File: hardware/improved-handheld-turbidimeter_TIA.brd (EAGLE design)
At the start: 30.1 x 39.4 mm, 11 parts

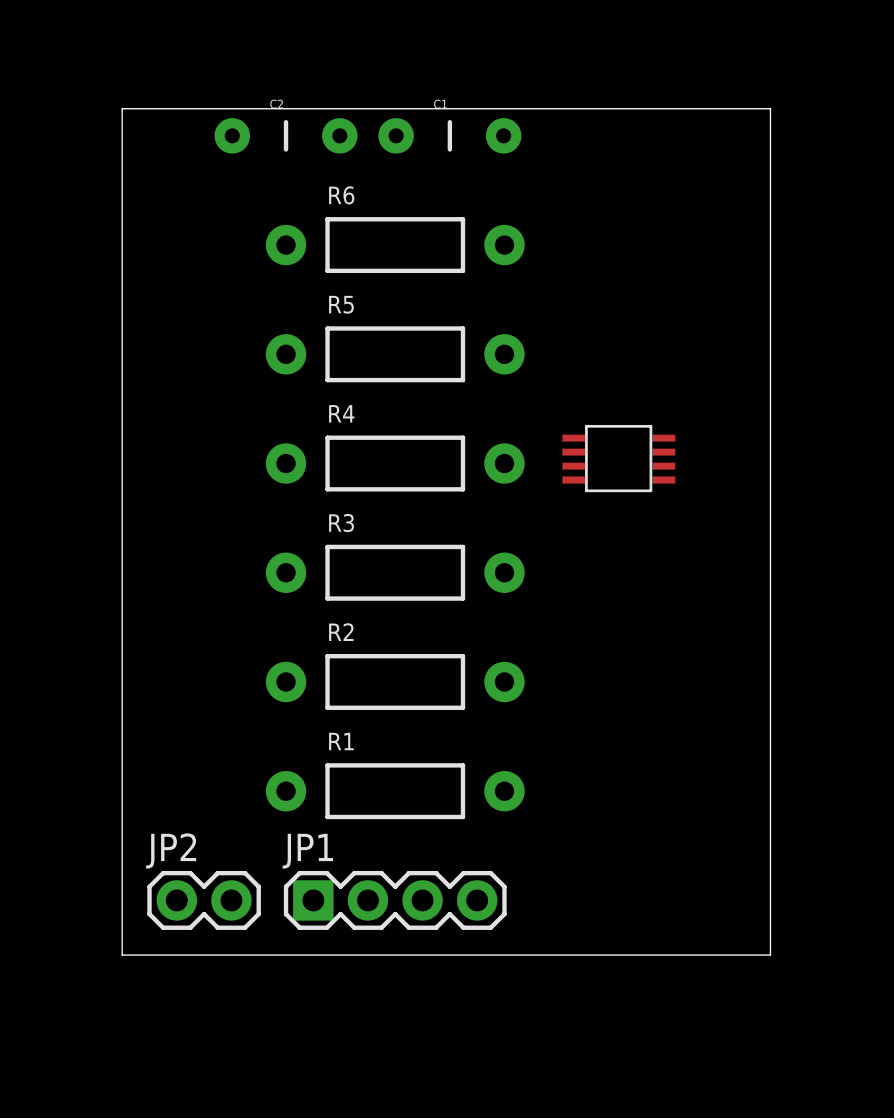
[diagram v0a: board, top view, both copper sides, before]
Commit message: basic TIA board routed
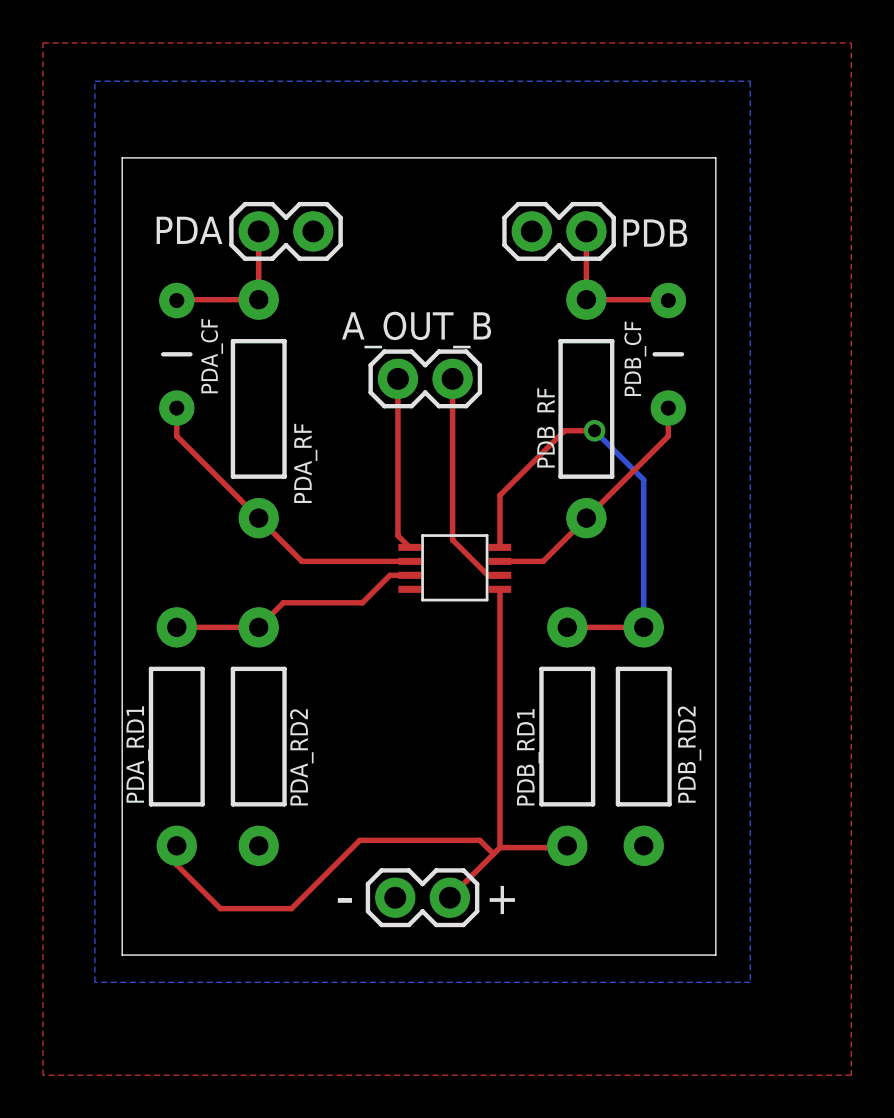
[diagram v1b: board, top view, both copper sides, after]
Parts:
- removed C1, C2: (no value), SparkFun-Passives:CAP-PTH-5MM
- removed JP1: (no value), SparkFun-Connectors:1X04
- removed JP2: (no value), SparkFun-Connectors:1X02
- removed R1, R2, R3, R4, R5, R6: (no value), SparkFun-Passives:AXIAL-0.4
- added A_OUT_B, JP3, PDA, PDB: (no value), SparkFun-Connectors:1X02
- added PDA_CF, PDB_CF: (no value), SparkFun-Passives:CAP-PTH-5MM
- added PDA_RD1, PDA_RD2, PDA_RF, PDB_RD1, PDB_RD2, PDB_RF: (no value), SparkFun-Passives:AXIAL-0.4
- moved U$1 9.16 mm to (14.0, 16.5)
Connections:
- net GND: now also JP3.2, PDA.2, PDA_RD2.P$1, PDB.1, PDB_RD2.P$1; no longer JP1.2, R4.P$1, R6.P$1
- net N$1: now also PDA.1, PDA_CF.2, PDA_RF.P$1; no longer C1.2, JP2.2, R1.P$1
- net N$2: now also PDA_CF.1, PDA_RF.P$2; no longer C1.1, R1.P$2
- net N$3: now also PDB.2, PDB_CF.2, PDB_RF.P$1; no longer C2.2, JP2.1, R2.P$1
- net N$4: now also PDB_CF.1, PDB_RF.P$2; no longer C2.1, R2.P$2
- net N$5: now also PDA_RD1.P$2, PDA_RD2.P$2; no longer R3.P$2, R4.P$2
- net N$6: now also PDB_RD1.P$2, PDB_RD2.P$2; no longer R5.P$2, R6.P$2
- net OUTA: now also A_OUT_B.1; no longer JP1.3
- net OUTB: now also A_OUT_B.2; no longer JP1.4
- net VCC: now also JP3.1, PDA_RD1.P$1, PDB_RD1.P$1; no longer JP1.1, R3.P$1, R5.P$1
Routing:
- net VCC: track 0.00 -> 36.5 mm
- net N$6: track 0.00 -> 21.7 mm, vias 0 -> 1
- net N$2: track 0.00 -> 14.6 mm
- net N$5: track 0.00 -> 11.8 mm
- net N$4: track 0.00 -> 11.6 mm
- net OUTB: track 0.00 -> 10.4 mm
- net OUTA: track 0.00 -> 8.06 mm
- net N$1: track 0.00 -> 7.00 mm
- net N$3: track 0.00 -> 7.00 mm
- added copper zone on layer 1, net GND
- added copper zone on layer 16, net GND
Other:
- board size 30.1 x 39.4 mm -> 27.6 x 37.1 mm
- board text added: "+"
- board text added: "-"
- board text added: "AWQUA TIA Board v1.0 2016/08/24"
